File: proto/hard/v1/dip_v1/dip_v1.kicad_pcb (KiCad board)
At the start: 2 copper layers, 100 x 100 mm, 79 parts, among them J1 RJ12, J10 Conn_01x04_Female, J11 Conn_01x02_Male, J12 Conn_01x04_Female, J13 Conn_01x09_Male, J14 Conn_02x02_Counter_Clockwise, J2 RJ12, J3 RJ12, J4 RJ12, J5 Conn_01x04_Female, J6 RJ45, J7 AudioJack3, J8 Conn_01x04_Female, J9 Conn_01x05_Male, Q1 2N7000, Q2 2N7000, Q3 2N7000, Q4 BS250, Q5 BS250, Q6 2N7000, Q7 BS250, U1 BluePill, U2 LM339, U3 ST485EBDR, U4 74HC595, U5 ULN2803A, U6 74HC04, U7 LM358

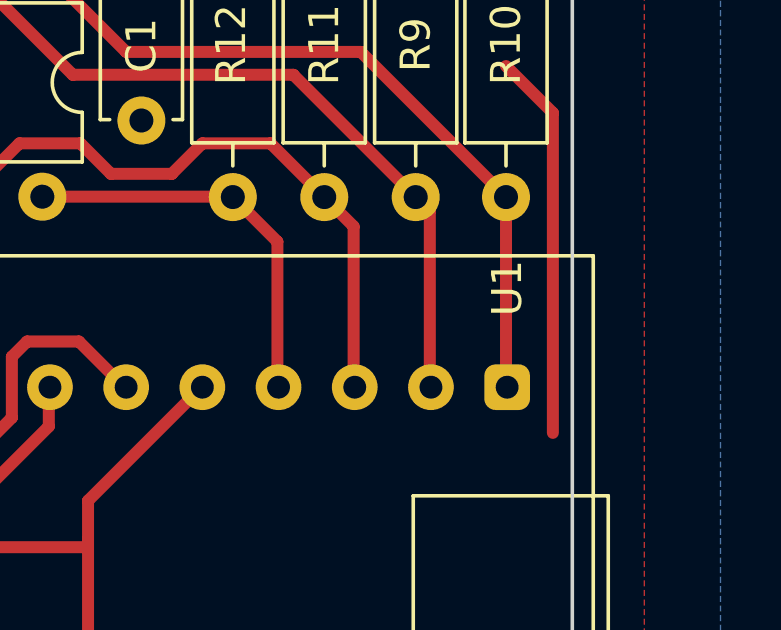
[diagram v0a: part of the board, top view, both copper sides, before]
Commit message: Added example project with button connection schematic only. Corrected "dip" pins assignment to comply with main project.
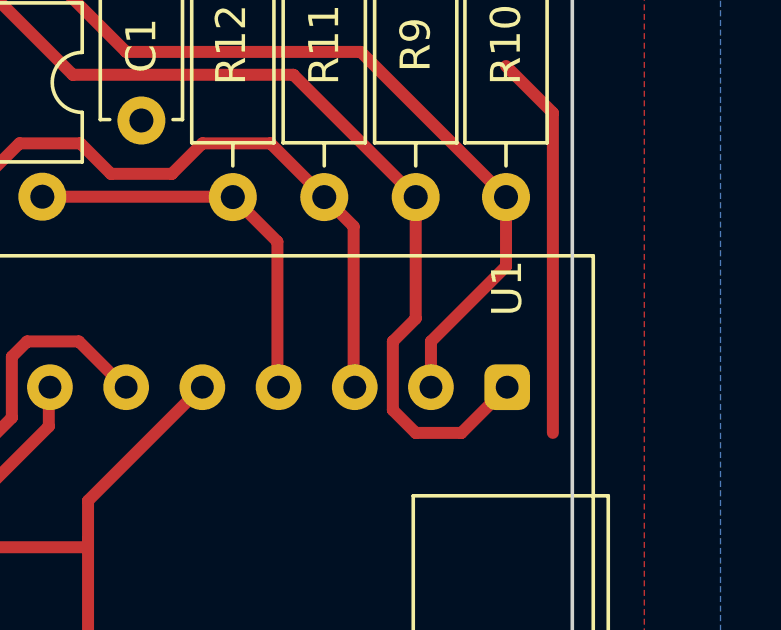
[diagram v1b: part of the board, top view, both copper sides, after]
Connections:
- R10 pad 2: /But0 -> /But1
- R9 pad 2: /But1 -> /But0
- U2 pad 1: /But0 -> /But1
- U2 pad 2: /But1 -> /But0
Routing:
- net /But0: track 25.0 -> 30.3 mm
- net /But1: track 24.7 -> 26.0 mm
